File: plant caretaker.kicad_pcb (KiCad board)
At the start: 2 copper layers, 56 parts, among them J3 Water_Pump, J4 Kitronik, J5 694106402002, Q1 FDMS86255, U1 UDA1380HN_N2, U2 TMP175AIDR, U4 LM2596S-5, U5 PAM8403D, U6 ESP32_C3_ZERO

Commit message: Added more connections
Updated footprints for pin heads and speakers
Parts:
- added LS1: Speaker, Connector_PinHeader_2.00mm:PinHeader_1x02_P2.00mm_Vertical_SMD_Pin1Left, F.Cu at (127.3, 54.2)
- added LS2: Speaker, Connector_PinHeader_2.00mm:PinHeader_1x02_P2.00mm_Vertical_SMD_Pin1Left, F.Cu at (123.5, 105.8)
- C10, C15, C21, C5, C6, C7, R11, R4, R6, R8, R9: moved to B.Cu
- J3: footprint Connector_PinHeader_1.00mm:PinHeader_1x02_P1.00mm_Vertical_SMD_Pin1Right -> Connector_PinHeader_2.00mm:PinHeader_1x02_P2.00mm_Vertical_SMD_Pin1Left
- J4: footprint Connector_PinHeader_1.00mm:PinHeader_1x03_P1.00mm_Vertical_SMD_Pin1Left -> Connector_PinHeader_2.00mm:PinHeader_1x03_P2.00mm_Vertical_SMD_Pin1Left
- moved U5 138.4 mm to (95.0, 70.8)
- moved C12 136.9 mm to (87.0, 75.2)
- moved R7 126.7 mm to (101.8, 74.2), turned to -90 degrees
- moved FB2 126.1 mm to (107.2, 90.4), turned to 90 degrees
- moved R9 124.1 mm to (106.0, 84.5), turned to 90 degrees
- moved C15 123.9 mm to (118.5, 89.5), turned to 90 degrees
- moved FB1 122.7 mm to (107.5, 78.5), turned to -90 degrees
- moved R11 122.0 mm to (112.0, 95.2), turned to 180 degrees
- moved C16 119.7 mm to (112.2, 74.8), turned to 180 degrees
- moved R8 119.5 mm to (108.3, 74.0), turned to 180 degrees
- moved R4 118.6 mm to (107.8, 94.0), turned to 90 degrees
- moved C6 118.4 mm to (106.0, 93.5), turned to 90 degrees
- moved C22 117.9 mm to (111.8, 93.5), turned to 90 degrees
- moved R6 116.2 mm to (106.2, 87.8), turned to 90 degrees
- moved C5 115.9 mm to (112.5, 98.2), turned to -90 degrees
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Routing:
- net +3V3: track 15.1 -> 49.2 mm
- net Net-(U5-INL): track 0.00 -> 25.1 mm, vias 0 -> 1
- net GND: track 55.3 -> 79.4 mm, vias 5 -> 9
- net /AudioCodec/A1: track 0.00 -> 19.9 mm, vias 0 -> 1
- net Net-(C15-Pad2): track 0.00 -> 18.6 mm
- net /AudioCodec/VDDA: track 0.00 -> 15.0 mm, vias 0 -> 1
- net /AudioAmplifier/R_IN: track 0.00 -> 13.4 mm
- net /AudioCodec/VADCP: track 0.00 -> 13.0 mm
- net /CODEC.DATAI: track 30.6 -> 18.4 mm
- net Net-(U1-SYSCLK): track 25.0 -> 13.2 mm
- net Net-(C21-Pad2): track 0.00 -> 10.8 mm, vias 0 -> 1
- net Net-(C16-Pad2): track 0.00 -> 10.3 mm
- net /CODEC.WSI: track 29.0 -> 19.2 mm
- net /CODEC.BCKI: track 31.4 -> 22.2 mm
- net /BuckConverter/12V: track 3.15 -> 11.0 mm, vias 1 -> 2
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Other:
- board outline added: 61.8 x 117 mm

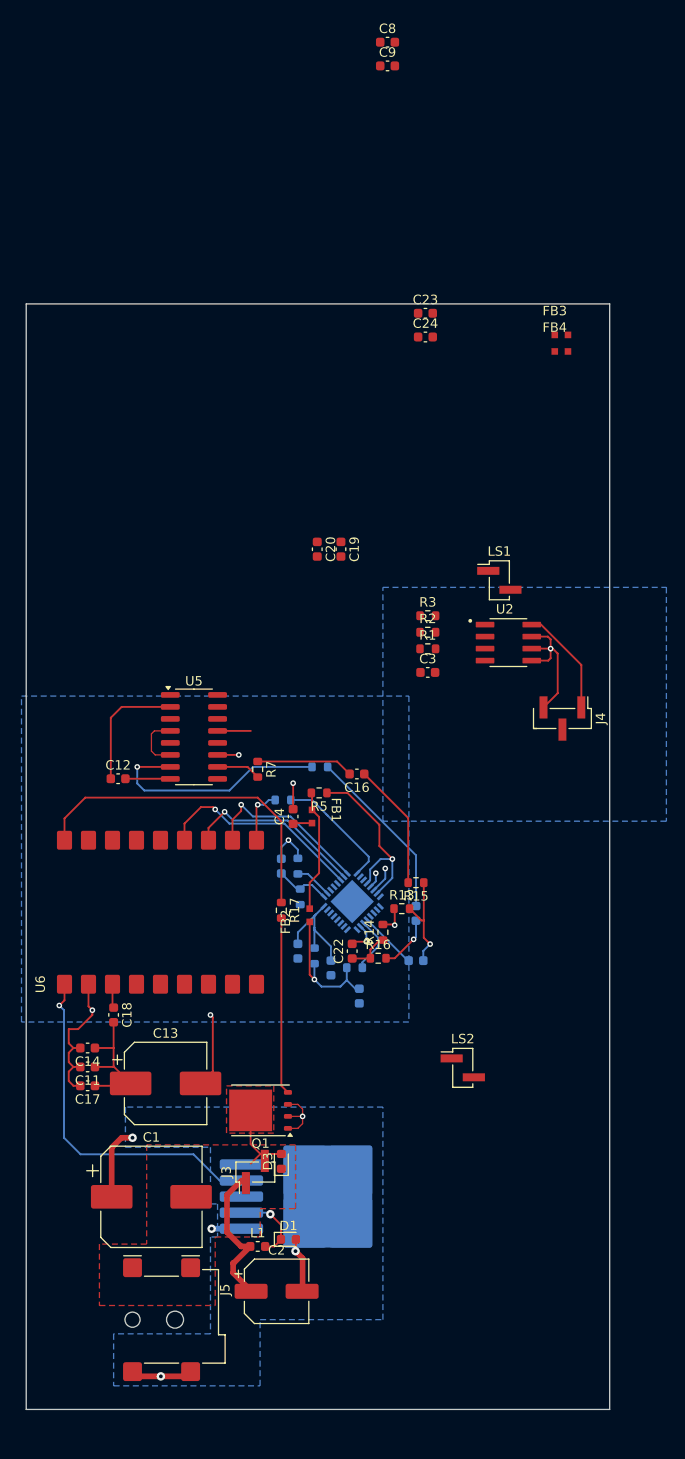
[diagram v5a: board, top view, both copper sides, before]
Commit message: Only I2C signals left + cleanup
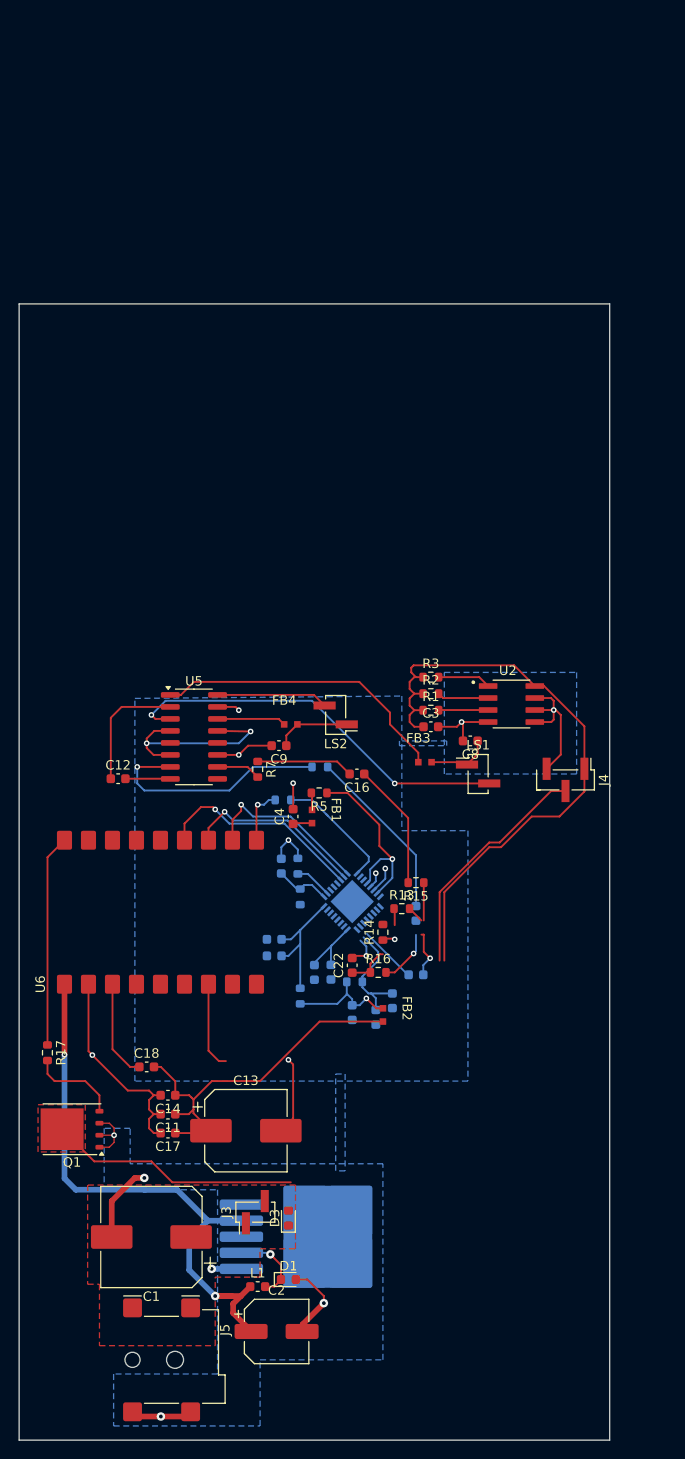
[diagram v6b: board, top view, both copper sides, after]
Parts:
- C19, C20, C23, C24: moved to B.Cu
- moved C8 74.5 mm to (124.2, 71.2), turned to 180 degrees
- moved C9 72.9 mm to (104.0, 71.8), turned to 180 degrees
- moved C23 70.4 mm to (109.5, 95.7), turned to 90 degrees
- moved C24 68.3 mm to (107.8, 95.8), turned to 90 degrees
- moved C20 49.9 mm to (114.2, 100.5), turned to 90 degrees
- moved FB4 48.8 mm to (104.5, 69.5)
- moved C19 48.1 mm to (116.0, 98.8), turned to 90 degrees
- moved FB3 47.5 mm to (118.8, 73.5)
- moved LS2 39.7 mm to (110.0, 68.5), turned to 180 degrees
- moved R17 29.0 mm to (79.5, 104.2)
- moved LS1 20.6 mm to (125.1, 74.8)
- moved Q1 20.0 mm to (82.1, 112.3)
- moved FB2 12.0 mm to (115.0, 99.5), turned to -90 degrees
- moved C11 9.86 mm to (92.2, 110.8)
- moved C13 9.86 mm to (100.5, 112.5)
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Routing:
- net +3V3: track 49.2 -> 129.5 mm, vias 0 -> 2
- net Net-(U5-LOUT-): track 0.00 -> 42.2 mm, vias 0 -> 2
- net Net-(J4-Pin_2): track 0.00 -> 34.4 mm
- net Net-(U5-LOUT+): track 0.00 -> 31.7 mm
- net GND: track 79.4 -> 110.3 mm, vias 9 -> 11
- net Net-(D3-A): track 8.72 -> 26.5 mm
- net /BuckConverter/PWM_IN: track 35.8 -> 22.4 mm
- net Net-(U5-ROUT+): track 0.00 -> 11.8 mm
- net Net-(Q1-G): track 18.7 -> 9.55 mm
- net /BuckConverter/5V_OUT: track 52.9 -> 61.9 mm, vias 1 -> 2
- net Net-(U6-3V3_OUT): track 2.52 -> 10.5 mm
- net Net-(C9-Pad1): track 0.00 -> 7.96 mm
- net /BuckConverter/12V: track 11.0 -> 3.15 mm, vias 2 -> 1
- net /AudioCodec/VREF: track 0.00 -> 7.33 mm
- net Net-(U5-ROUT-): track 0.00 -> 7.29 mm
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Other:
- board size 61.8 x 117 mm -> 62.5 x 120.2 mm

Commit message: Different version of connections
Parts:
- C15, C19, C20, C21, C5, C6, C7, R11, R4, R8: moved to F.Cu
- C4: moved to B.Cu
- moved R3 73.7 mm to (62.2, 110.2), turned to 90 degrees
- moved R2 71.2 mm to (64.0, 110.2), turned to 90 degrees
- moved FB1 63.3 mm to (46.0, 93.7), turned to 90 degrees
- moved R6 63.2 mm to (43.2, 92.5), turned to 0 degrees
- moved C4 62.9 mm to (43.2, 88.5), turned to 0 degrees
- moved R9 62.8 mm to (43.2, 86.8), turned to 180 degrees
- moved C10 61.3 mm to (43.2, 90.8), turned to 0 degrees
- moved U1 59.1 mm to (52.8, 91.5)
- moved R4 59.1 mm to (47.2, 101.5)
- moved C5 58.3 mm to (53.5, 102.2), turned to 90 degrees
- moved C19 58.1 mm to (58.0, 102.2)
- moved R11 56.8 mm to (55.5, 102.2), turned to -90 degrees
- moved C23 56.7 mm to (52.8, 97.0), turned to 180 degrees
- moved FB2 56.6 mm to (60.1, 113.2), turned to 0 degrees
- moved C24 55.0 mm to (52.8, 98.8), turned to 180 degrees
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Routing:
- net +3V3: track 129.5 -> 71.6 mm, vias 2 -> 0
- net /AudioCodec/SCL: track 7.10 -> 52.7 mm, vias 1 -> 2
- net /AudioCodec/SDA: track 8.43 -> 51.9 mm, vias 1 -> 2
- net Net-(U5-LOUT-): track 42.2 -> 0.00 mm, vias 2 -> 0
- net /CODEC.SYSCLK: track 5.87 -> 45.3 mm
- net /CODEC.WSI: track 19.2 -> 56.0 mm
- net /CODEC.BCKI: track 22.2 -> 58.2 mm
- net /CODEC.DATAI: track 18.4 -> 54.0 mm
- net Net-(U5-LOUT+): track 31.7 -> 0.00 mm
- net /BuckConverter/PWM_IN: track 22.4 -> 0.00 mm
- net GND: track 110.3 -> 132.2 mm
- net Net-(J4-Pin_2): track 34.4 -> 12.8 mm
- net Net-(U5-INL): track 25.1 -> 4.96 mm, vias 1 -> 0
- net Net-(U6-3V3_OUT): track 10.5 -> 28.2 mm
- net /AudioCodec/VDDA: track 12.1 -> 25.2 mm, vias 1 -> 0
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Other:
- board size 62.5 x 120.2 mm -> 106.2 x 88 mm

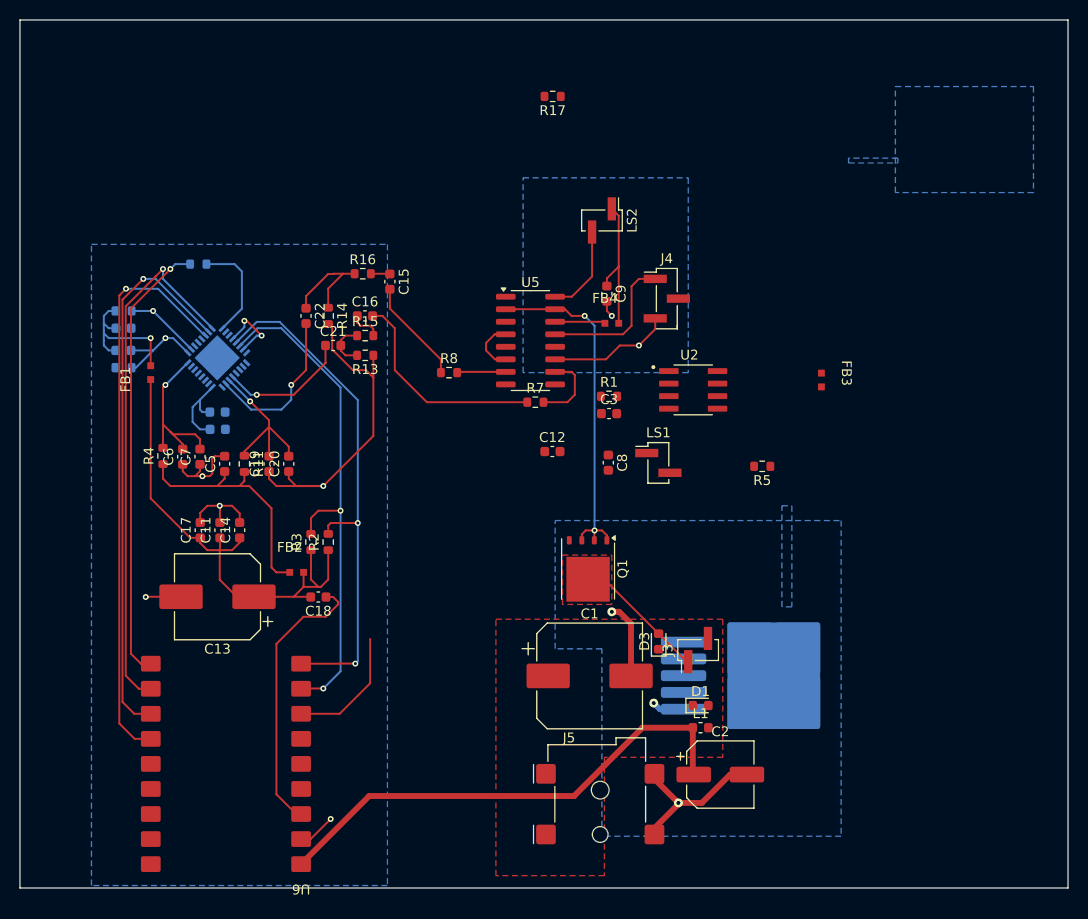
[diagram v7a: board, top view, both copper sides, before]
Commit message: Finished PCB
Also added GNDA and GNDD references, to be changed back to GND later. Also added wires connecting ground polygons
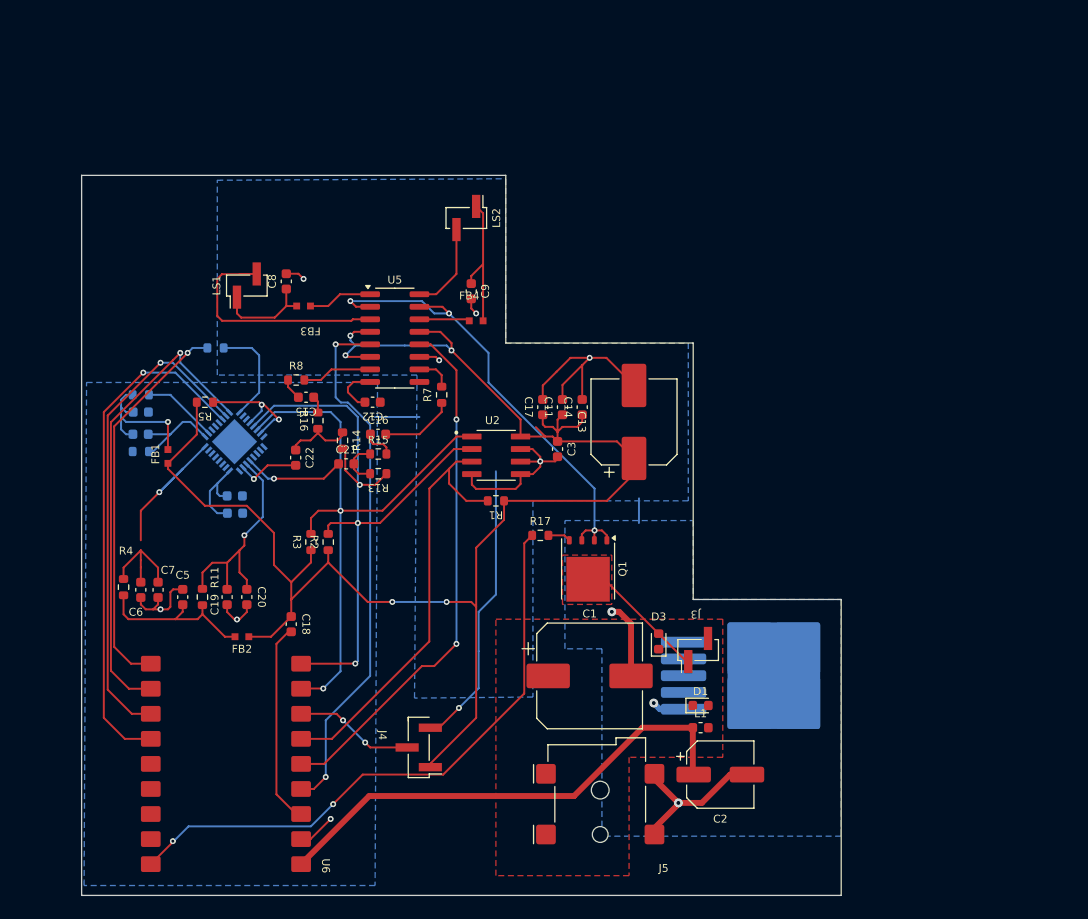
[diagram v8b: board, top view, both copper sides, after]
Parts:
- moved R5 56.9 mm to (51.5, 96.0)
- moved FB3 52.2 mm to (62.2, 86.2), turned to 180 degrees
- moved J4 52.0 mm to (73.2, 131.0), turned to 180 degrees
- moved C13 45.8 mm to (95.0, 98.0), turned to 90 degrees
- moved LS1 45.4 mm to (55.8, 84.2), turned to 90 degrees
- moved R17 44.5 mm to (85.5, 109.5), turned to 0 degrees
- moved C8 37.5 mm to (59.8, 83.8), turned to 90 degrees
- moved C11 36.9 mm to (87.8, 96.5)
- moved C14 36.9 mm to (89.8, 96.5)
- moved C17 36.9 mm to (85.8, 96.5)
- moved U2 21.0 mm to (81.0, 101.4)
- moved C12 18.9 mm to (68.5, 96.0), turned to 180 degrees
- moved R1 15.6 mm to (81.0, 106.0), turned to 180 degrees
- moved R16 15.6 mm to (63.0, 97.9), turned to 90 degrees
- moved R8 15.5 mm to (60.8, 93.8)
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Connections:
- C11 pad 2: GND -> GNDA
- C12 pad 1: GND -> GNDA
- C13 pad 2: GND -> GNDA
- C14 pad 2: GND -> GNDA
- C17 pad 2: GND -> GNDA
- C19 pad 1: GND -> GNDD
- C20 pad 1: GND -> GNDD
- C23 pad 1: GND -> GNDD
- C24 pad 1: GND -> GNDD
- C3 pad 2: GND -> GNDA
- C4 pad 2: GND -> GNDD
- C5 pad 2: GND -> GNDD
- C6 pad 1: GND -> GNDD
- C7 pad 1: GND -> GNDD
- C8 pad 2: GND -> GNDA
- C9 pad 2: GND -> GNDA
- J4 pad 3: GND -> GNDA
- R13 pad 1: GND -> GNDD
- R14 pad 2: GND -> GNDD
- R6 pad 1: GND -> GNDD
- U1 pad 10: GND -> GNDD
- U1 pad 11: GND -> GNDD
- U1 pad 16: GND -> GNDD
- U1 pad 18: GND -> GNDD
- U1 pad 20: GND -> GNDD
- U1 pad 24: GND -> GNDD
- U1 pad 26: GND -> GNDD
- U1 pad 27: GND -> GNDD
- U1 pad 28: GND -> GNDD
- U1 pad 29: GND -> GNDD
- U1 pad 30: GND -> GNDD
- U1 pad 31: GND -> GNDD
- U1 pad 33: GND -> GNDD
- U2 pad 4: GND -> GNDA
- U2 pad 5: GND -> GNDA
- U2 pad 6: GND -> GNDA
- U2 pad 7: GND -> GNDA
- U5 pad 11: GND -> GNDA
- U6 pad 2: GND -> GNDD
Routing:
- net +3V3: track 71.6 -> 166.5 mm, vias 0 -> 5
- net GNDA: track 0.00 -> 74.0 mm, vias 0 -> 6
- net /BuckConverter/PWM_IN: track 0.00 -> 61.4 mm, vias 0 -> 2
- net GND: track 132.2 -> 73.2 mm, vias 11 -> 5
- net /AudioAmplifier/MUTE_IN: track 0.00 -> 54.1 mm, vias 0 -> 2
- net /AudioAmplifier/SHDN_IN: track 0.00 -> 53.4 mm, vias 0 -> 2
- net /TempSensor/ALERT: track 0.00 -> 44.2 mm
- net GNDD: track 0.00 -> 23.8 mm, vias 0 -> 4
- net Net-(U5-LOUT-): track 0.00 -> 23.7 mm
- net Net-(C16-Pad2): track 21.8 -> 7.53 mm
- net Net-(U1-VOUTL): track 16.5 -> 6.43 mm
- net Net-(C8-Pad1): track 0.00 -> 10.1 mm
- net /AudioCodec/SDA: track 51.9 -> 61.0 mm
- net /AudioCodec/VADCP: track 17.4 -> 26.3 mm
- net Net-(C15-Pad2): track 10.6 -> 2.18 mm
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- added copper zone on B.Cu, net GNDA
- added copper zone on B.Cu, net GNDD
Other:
- board size 106.2 x 88 mm -> 77 x 73 mm
- rule solder_mask_min_width: 0.12 -> 0.1
